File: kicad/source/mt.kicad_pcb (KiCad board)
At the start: 4 copper layers, 132 parts, among them IC1 MCP73831T-2ACI_OT, IC10 SN74HC148NSR, IC11 SN74HC148NSR, IC2 BQ29728DSER, IC3 TLV74333PDBVR, IC4 TLV9152IDR, IC5 MSPM0G3507SPMR, IC6 IS62WV1288BLL-55QLI, IC7 DAC082S085CIMMX_NOPB, IC8 SN74HC148NSR, IC9 SN74HC148NSR, J1 694106301002, J2 3557-2, J3 SJ1-3524N, J4 Conn_01x05_Pin, J5 Conn_01x09_Pin, J6 Conn_01x03_Pin, J7 Conn_01x03_Pin, J8 Conn_01x03_Pin, Q1 CSD16406Q3, Q2 CSD16406Q3, U1 1043

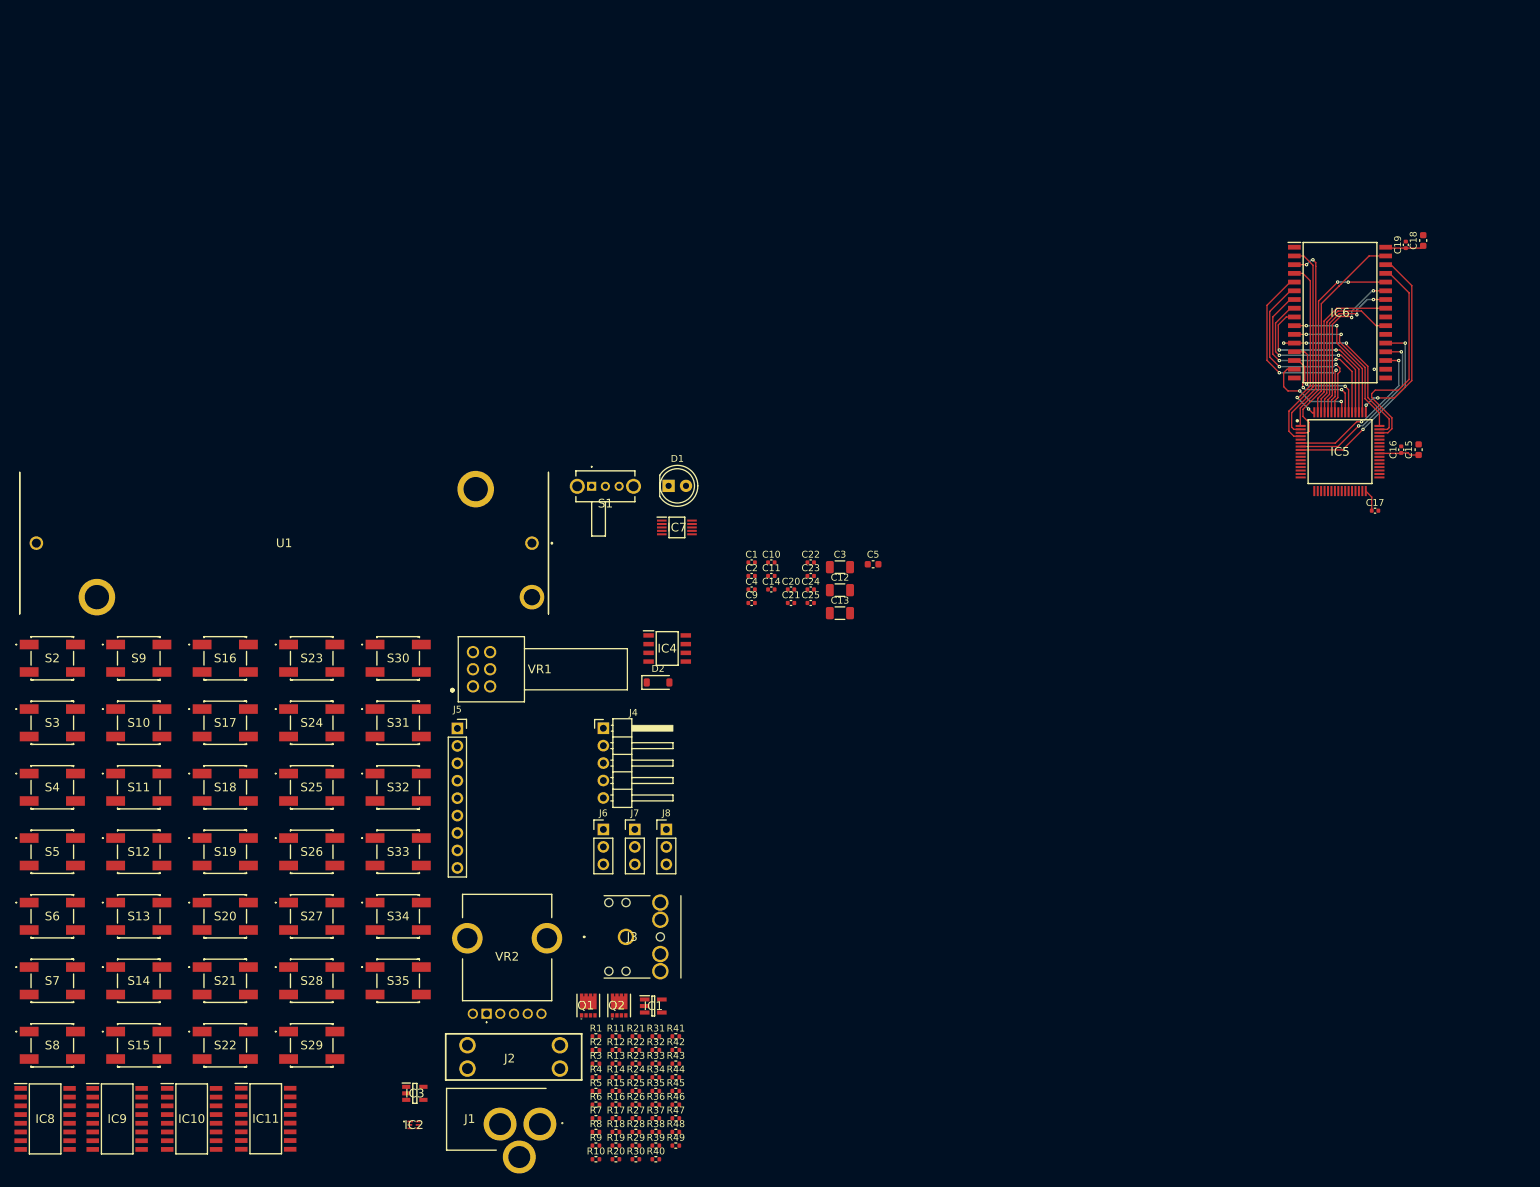
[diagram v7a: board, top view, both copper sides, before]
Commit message: completed SRAM routing, started power electronics routing
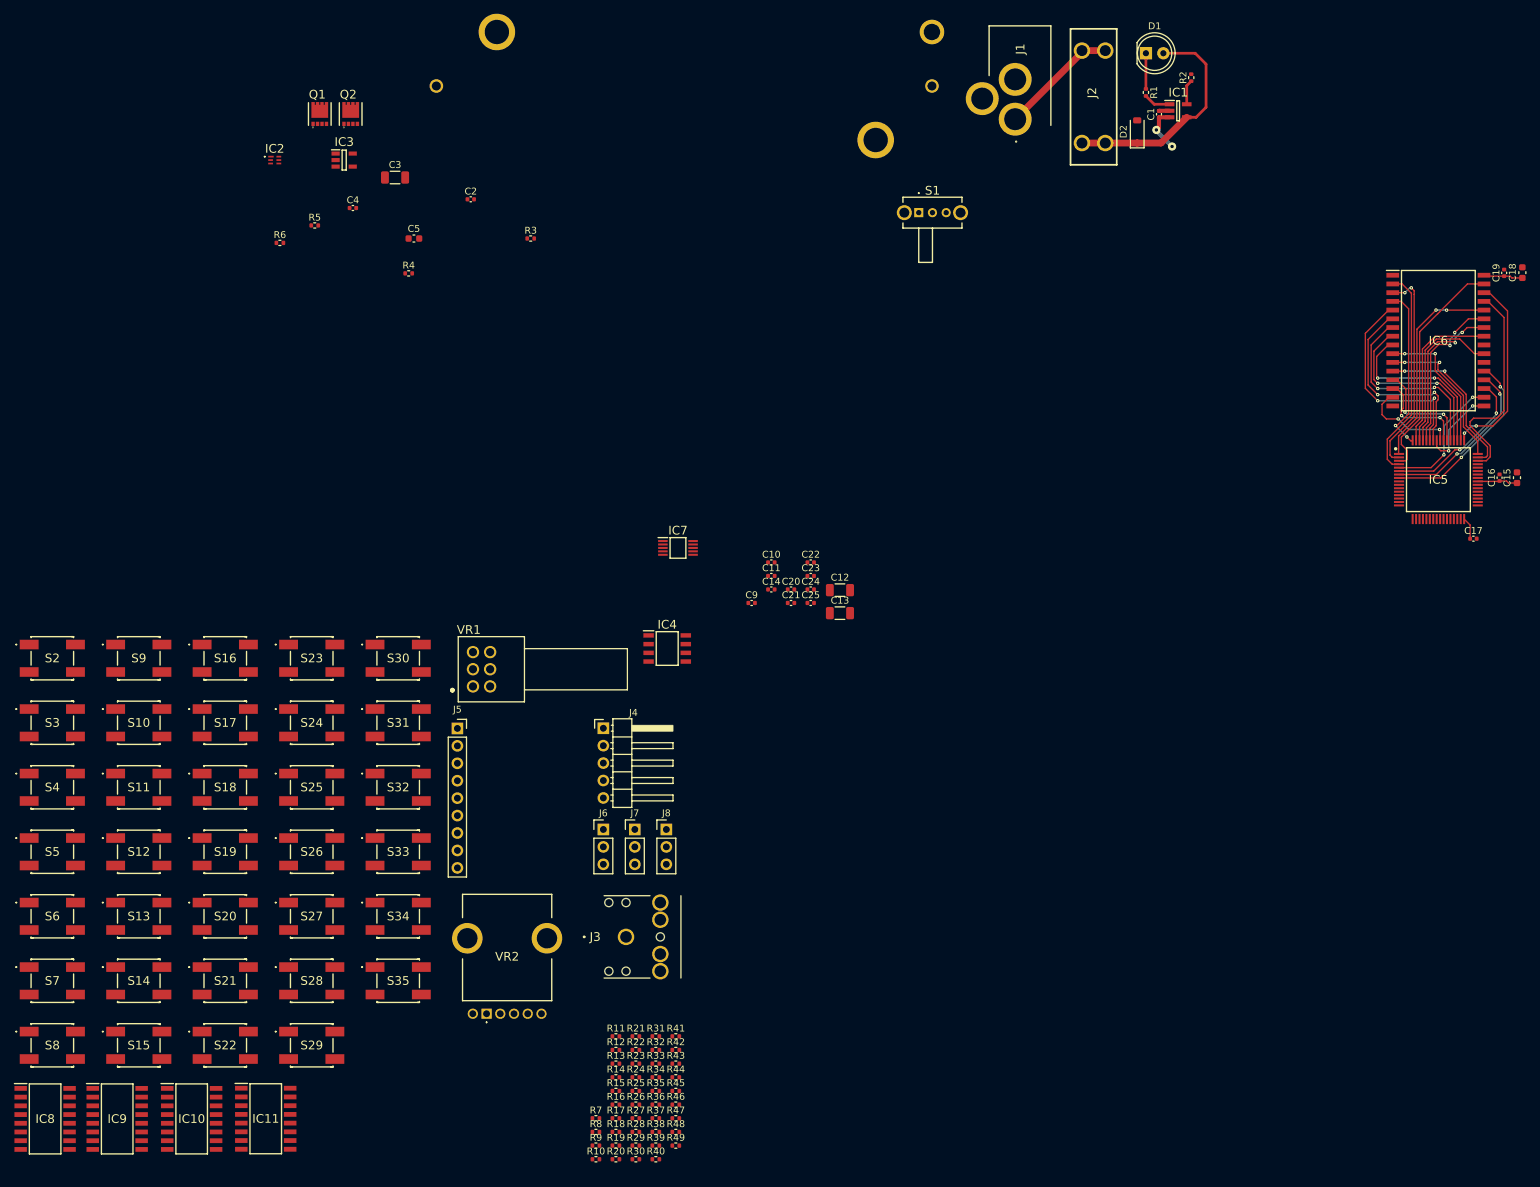
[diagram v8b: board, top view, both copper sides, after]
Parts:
- U1: moved to B.Cu
- moved J1 181.9 mm to (165.7, 23.6), turned to -90 degrees
- moved R2 166.1 mm to (195.2, 31.2), turned to 90 degrees
- moved J2 163.4 mm to (181.0, 34.0), turned to -90 degrees
- moved R1 159.2 mm to (188.6, 33.3), turned to -90 degrees
- moved IC1 151.2 mm to (193.3, 36.0)
- moved IC2 142.1 mm to (61.6, 43.2)
- moved IC3 136.4 mm to (71.8, 43.2)
- moved Q1 135.7 mm to (68.2, 36.5)
- moved Q2 135.7 mm to (72.7, 36.5)
- moved R6 133.8 mm to (62.4, 55.2)
- moved R5 132.6 mm to (67.5, 52.7)
- moved R3 120.6 mm to (98.9, 54.6)
- moved R4 120.3 mm to (81.2, 59.7)
- moved D2 106.4 mm to (187.3, 39.0), turned to 90 degrees
- moved D1 93.9 mm to (188.6, 27.6)
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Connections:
- Q1 pad 9: (no net) -> Net-(Q1-D_1)
- Q2 pad 9: (no net) -> Net-(Q1-D_1)
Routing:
- net Net-(D1-A): track 0.00 -> 33.4 mm
- net I/O4: track 0.00 -> 19.1 mm, vias 1 -> 2
- net Net-(J1-POWER): track 0.00 -> 17.4 mm
- net I/O3: track 0.00 -> 12.6 mm, vias 0 -> 2
- net CELL+: track 0.00 -> 6.88 mm, vias 0 -> 2
- net Net-(D1-K): track 0.00 -> 5.21 mm
- net Net-(IC1-STAT): track 0.00 -> 3.95 mm
- net Net-(IC1-PROG): track 0.00 -> 3.64 mm
- net A0: track 25.6 -> 24.0 mm, vias 3 -> 2
- net GND: track 0.00 -> 1.56 mm
- net I/O7: track 28.3 -> 27.0 mm
- net I/O6: track 25.8 -> 24.8 mm
- net I/O5: track 23.3 -> 22.5 mm
- net I/O0: track 16.2 -> 15.7 mm
